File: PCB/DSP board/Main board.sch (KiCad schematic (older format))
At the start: 5 parts, among them X1 Mini_PCI-e

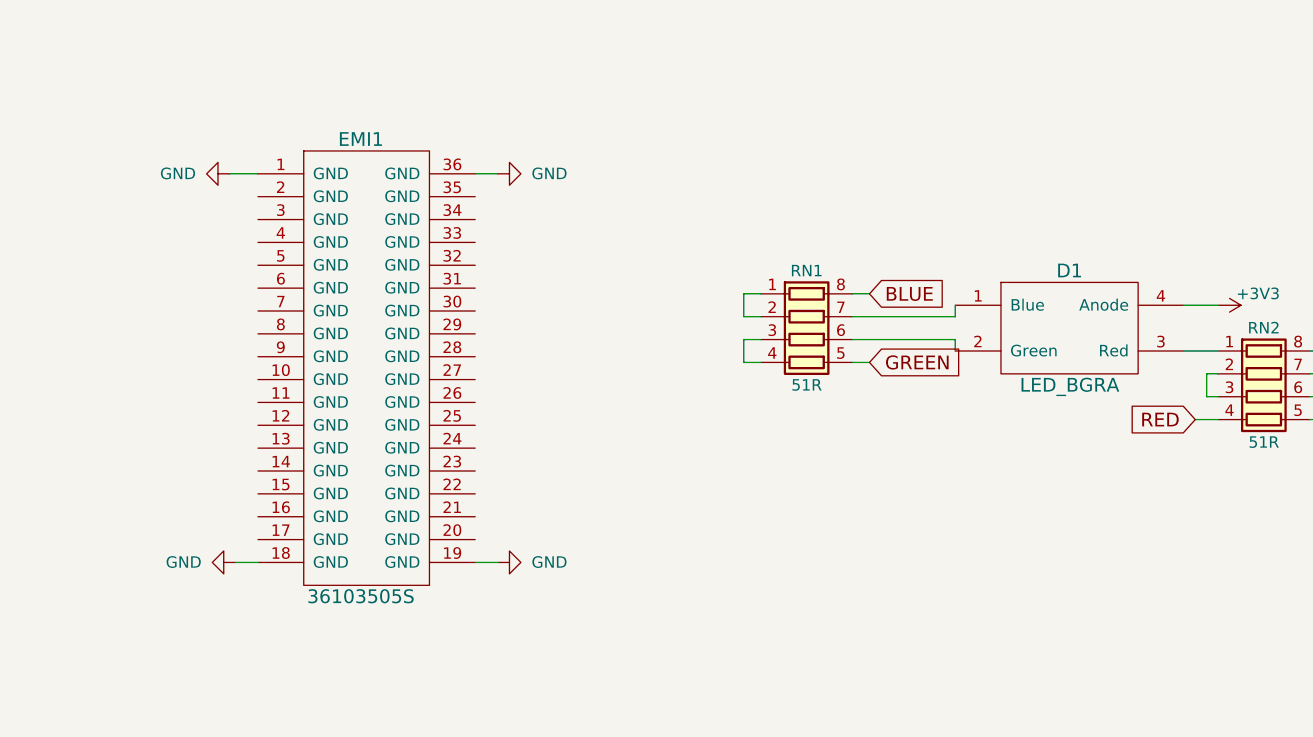
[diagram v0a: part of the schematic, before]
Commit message: Schematics + Footprints Rev.1
Ready to route.
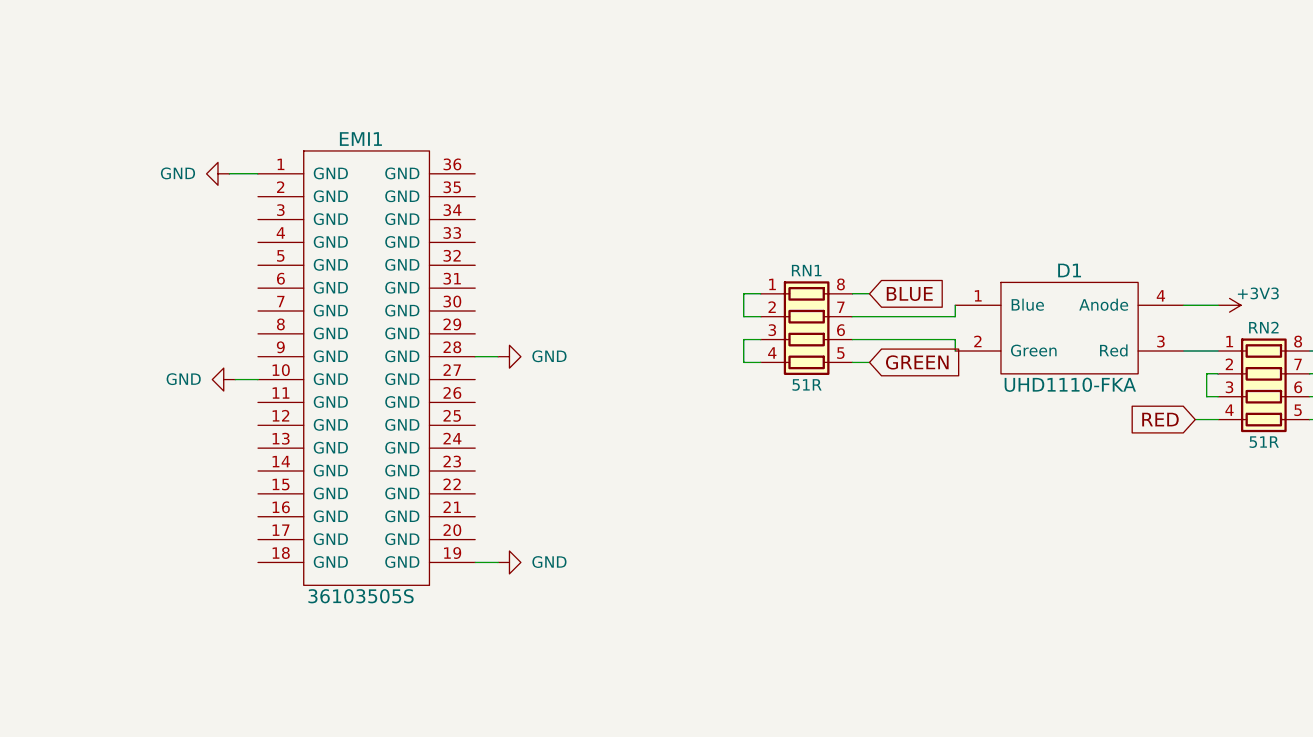
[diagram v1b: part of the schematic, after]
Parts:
- D1: value LED_BGRA -> UHD1110-FKA; footprint (none) -> LED:PLCC-4_1x1mm
- EMI1: footprint (none) -> EMI:36103505S
- RN1, RN2: footprint (none) -> Resistor:0603_RN4
- X1: footprint (none) -> PCI-e:Mini_PCI-e
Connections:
- net GND: now also EMI1.10 (GND), EMI1.28 (GND); no longer EMI1.18 (GND), EMI1.36 (GND)
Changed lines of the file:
@@
 F 0 "X1" H 2800 4400 60  0000 C CNN
 F 1 "Mini_PCI-e" H 2850 2500 60  0000 C CNN
-F 2 "" H 2700 2950 60  0001 C CNN
+F 2 "PCI-e:Mini_PCI-e" H 2700 2950 60  0001 C CNN
 F 3 "" H 2700 2950 60  0001 C CNN
 	1    2800 3450
@@
 F 0 "X1" H 2800 7150 60  0000 C CNN
 F 1 "Mini_PCI-e" H 2850 5250 60  0000 C CNN
-F 2 "" H 2700 5700 60  0001 C CNN
+F 2 "PCI-e:Mini_PCI-e" H 2700 5700 60  0001 C CNN
 F 3 "" H 2700 5700 60  0001 C CNN
 	2    2800 6200
@@
 HRTIM_EEV3
 $Comp
-L GND #PWR1
+L GND #PWR01
 U 1 1 5AB55A4F
 P 3275 2750
-F 0 "#PWR1" H 3275 2500 50  0001 C CNN
+F 0 "#PWR01" H 3275 2500 50  0001 C CNN
 F 1 "GND" V 3275 2525 50  0000 C CNN
 F 2 "" H 3275 2750 50  0001 C CNN
@@
 F 0 "EMI1" H 6075 5150 60  0000 C CNN
 F 1 "36103505S" H 6075 3150 60  0000 C CNN
-F 2 "" H 5575 3950 60  0001 C CNN
+F 2 "EMI:36103505S" H 5575 3950 60  0001 C CNN
 F 3 "" H 5575 3950 60  0001 C CNN
 	1    6075 4150
@@
 $EndComp
 $Comp
-L GND #PWR2
+L GND #PWR02
 U 1 1 5ABA06BB
 P 5500 3300
-F 0 "#PWR2" H 5500 3050 50  0001 C CNN
+F 0 "#PWR02" H 5500 3050 50  0001 C CNN
 F 1 "GND" V 5500 3075 50  0000 C CNN
 F 2 "" H 5500 3300 50  0001 C CNN
@@
 	5500 3300 5625 3300
 $Comp
-L GND #PWR3
+L GND #PWR03
 U 1 1 5ABA072B
-P 5525 5000
-F 0 "#PWR3" H 5525 4750 50  0001 C CNN
-F 1 "GND" V 5525 4775 50  0000 C CNN
-F 2 "" H 5525 5000 50  0001 C CNN
-F 3 "" H 5525 5000 50  0001 C CNN
-	1    5525 5000
+P 5525 4200
+F 0 "#PWR03" H 5525 3950 50  0001 C CNN
+F 1 "GND" V 5525 3975 50  0000 C CNN
+F 2 "" H 5525 4200 50  0001 C CNN
+F 3 "" H 5525 4200 50  0001 C CNN
+	1    5525 4200
 	0    1    1    0
 $EndComp
 $Comp
-L GND #PWR5
+L GND #PWR04
 U 1 1 5ABA0775
 P 6675 5000
-F 0 "#PWR5" H 6675 4750 50  0001 C CNN
+F 0 "#PWR04" H 6675 4750 50  0001 C CNN
 F 1 "GND" V 6675 4775 50  0000 C CNN
 F 2 "" H 6675 5000 50  0001 C CNN
@@
 $EndComp
 $Comp
-L GND #PWR4
+L GND #PWR05
 U 1 1 5ABA07D1
-P 6675 3300
-F 0 "#PWR4" H 6675 3050 50  0001 C CNN
-F 1 "GND" V 6675 3075 50  0000 C CNN
-F 2 "" H 6675 3300 50  0001 C CNN
-F 3 "" H 6675 3300 50  0001 C CNN
-	1    6675 3300
+P 6675 4100
+F 0 "#PWR05" H 6675 3850 50  0001 C CNN
+F 1 "GND" V 6675 3875 50  0000 C CNN
+F 2 "" H 6675 4100 50  0001 C CNN
+F 3 "" H 6675 4100 50  0001 C CNN
+	1    6675 4100
 	0    -1   -1   0
 $EndComp
 Wire Wire Line
-	6575 3300 6675 3300
+	6575 4100 6675 4100
 Wire Wire Line
 	6575 5000 6675 5000
 Wire Wire Line
-	5525 5000 5625 5000
+	5525 4200 5625 4200
 $Comp
 L LED_BGRA D1
@@
 P 9175 3975
 F 0 "D1" H 9175 4225 60  0000 C CNN
-F 1 "LED_BGRA" H 9175 3725 60  0000 C CNN
-F 2 "" H 8875 3975 60  0001 C CNN
+F 1 "UHD1110-FKA" H 9175 3725 60  0000 C CNN
+F 2 "LED:PLCC-4_1x1mm" H 8875 3975 60  0001 C CNN
 F 3 "" H 8875 3975 60  0001 C CNN
 	1    9175 3975
@@
 F 0 "RN1" V 7725 4025 50  0000 C CNN
 F 1 "51R" V 8225 4025 50  0000 C CNN
-F 2 "" V 8300 4025 50  0001 C CNN
+F 2 "Resistor:0603_RN4" V 8300 4025 50  0001 C CNN
 F 3 "" H 8025 4025 50  0001 C CNN
 	1    8025 4025
@@
 F 0 "RN2" V 9725 4275 50  0000 C CNN
 F 1 "51R" V 10225 4275 50  0000 C CNN
-F 2 "" V 10300 4275 50  0001 C CNN
+F 2 "Resistor:0603_RN4" V 10300 4275 50  0001 C CNN
 F 3 "" H 10025 4275 50  0001 C CNN
 	1    10025 4275
@@
 	9725 4375 9825 4375
 $Comp
-L +3V3 #PWR6
+L +3V3 #PWR06
 U 1 1 5AB3F000
 P 9825 3875
-F 0 "#PWR6" H 9825 3725 50  0001 C CNN
+F 0 "#PWR06" H 9825 3725 50  0001 C CNN
 F 1 "+3V3" V 9775 4050 50  0000 C CNN
 F 2 "" H 9825 3875 50  0001 C CNN

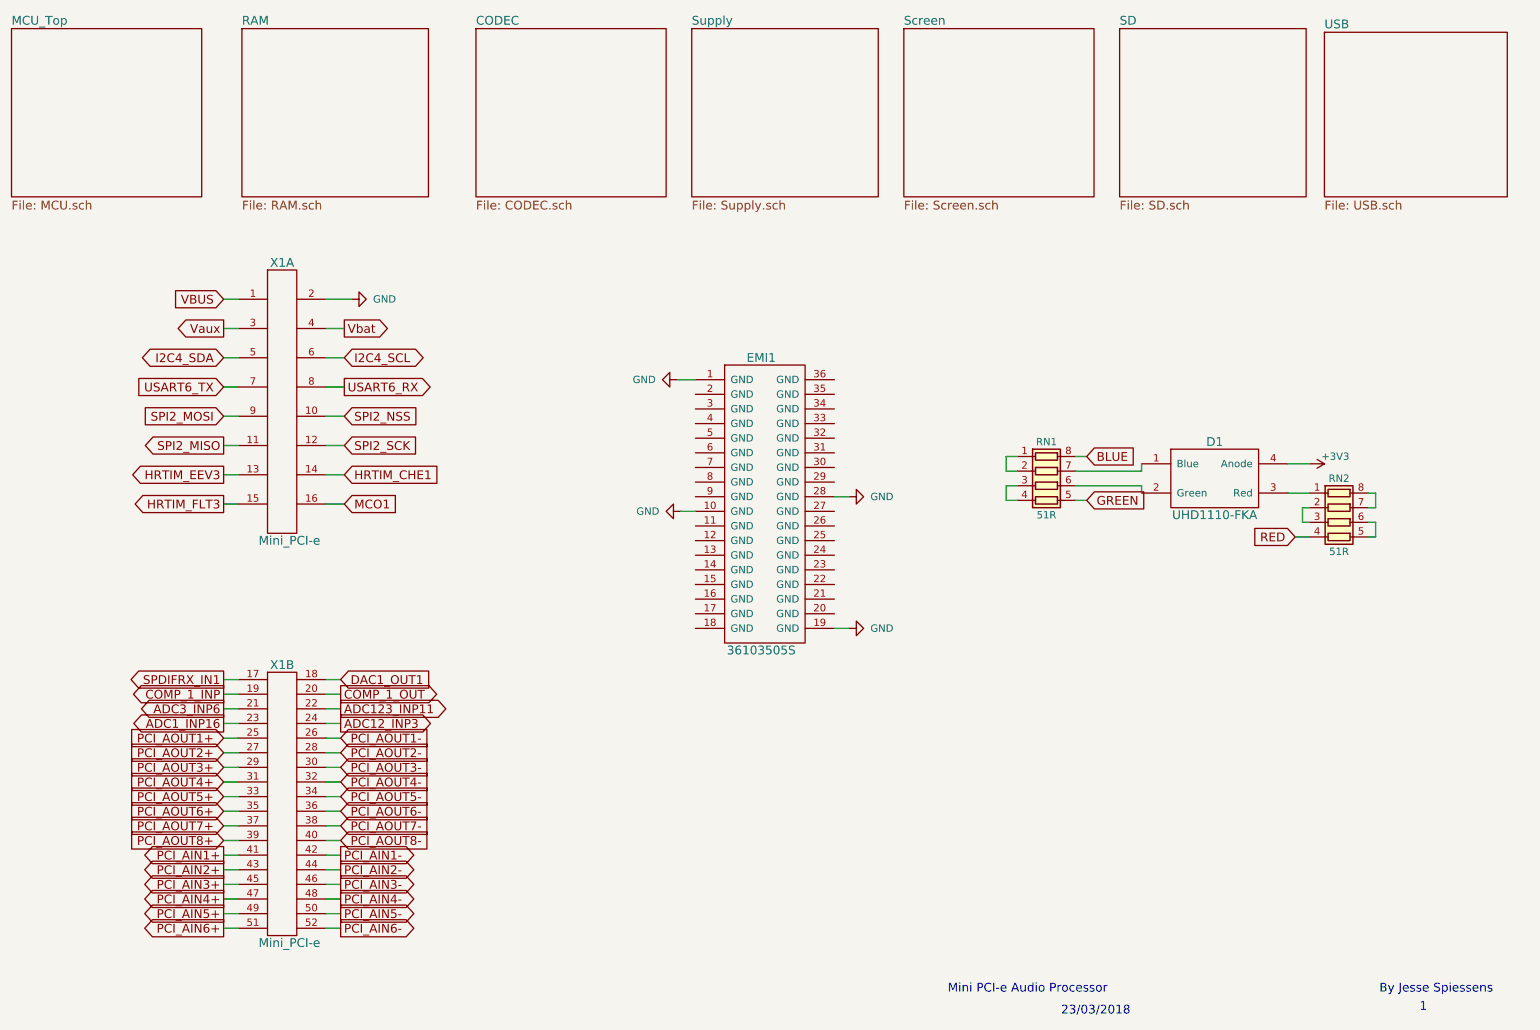
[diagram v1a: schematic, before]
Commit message: Schematics & PCB
Schematics update - ERC error fixing
PCB - setup & PCB outline
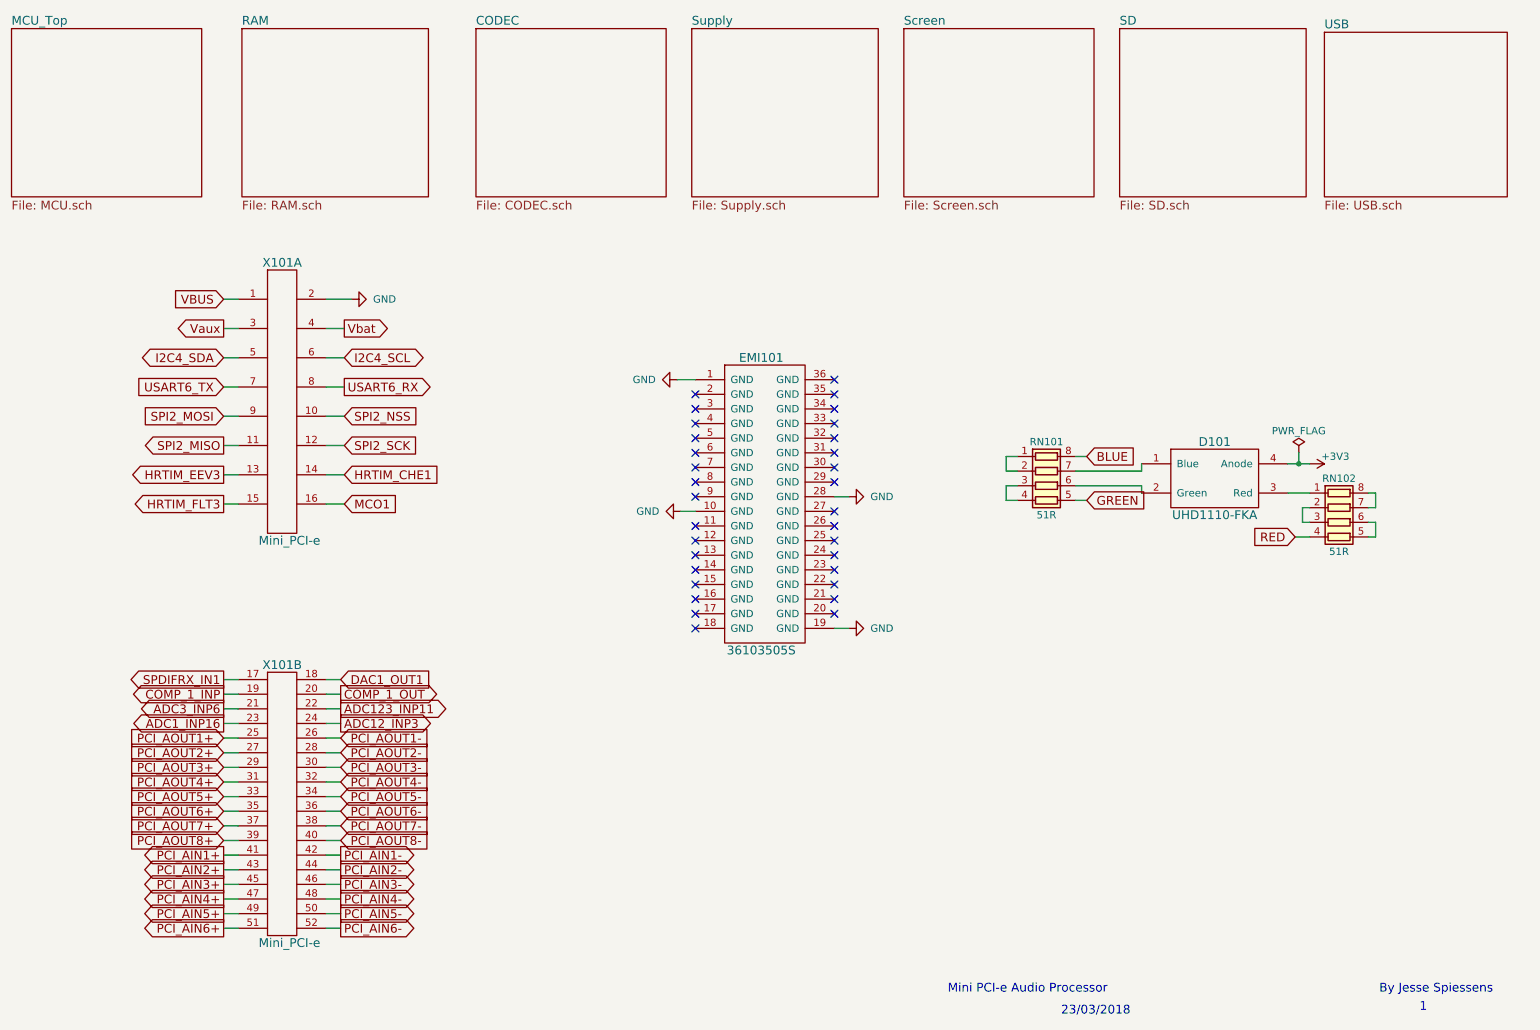
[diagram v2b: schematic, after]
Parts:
- renumbered D1 to D101, EMI1 to EMI101, RN1 to RN101, RN2 to RN102, X1 to X101
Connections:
- no-connect marks 0 -> 32
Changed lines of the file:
@@
 $EndSheet
 $Comp
-L Mini_PCI-e X1
+L Mini_PCI-e X101
 U 1 1 5AB547B6
 P 2800 3450
-F 0 "X1" H 2800 4400 60  0000 C CNN
+F 0 "X101" H 2800 4400 60  0000 C CNN
 F 1 "Mini_PCI-e" H 2850 2500 60  0000 C CNN
 F 2 "PCI-e:Mini_PCI-e" H 2700 2950 60  0001 C CNN
@@
 $EndComp
 $Comp
-L Mini_PCI-e X1
+L Mini_PCI-e X101
 U 2 1 5AB54885
 P 2800 6200
-F 0 "X1" H 2800 7150 60  0000 C CNN
+F 0 "X101" H 2800 7150 60  0000 C CNN
 F 1 "Mini_PCI-e" H 2850 5250 60  0000 C CNN
 F 2 "PCI-e:Mini_PCI-e" H 2700 5700 60  0001 C CNN
@@
 	3100 5350 3200 5350
 $Comp
-L 36103505S EMI1
+L 36103505S EMI101
 U 1 1 5ABA05A0
 P 6075 4150
-F 0 "EMI1" H 6075 5150 60  0000 C CNN
+F 0 "EMI101" H 6075 5150 60  0000 C CNN
 F 1 "36103505S" H 6075 3150 60  0000 C CNN
 F 2 "EMI:36103505S" H 5575 3950 60  0001 C CNN
@@
 	5525 4200 5625 4200
 $Comp
-L LED_BGRA D1
+L LED_BGRA D101
 U 1 1 5AB3DEEC
 P 9175 3975
-F 0 "D1" H 9175 4225 60  0000 C CNN
+F 0 "D101" H 9175 4225 60  0000 C CNN
 F 1 "UHD1110-FKA" H 9175 3725 60  0000 C CNN
 F 2 "LED:PLCC-4_1x1mm" H 8875 3975 60  0001 C CNN
@@
 $EndComp
 $Comp
-L R_Pack04 RN1
+L R_Pack04 RN101
 U 1 1 5AB3E0B3
 P 8025 4025
-F 0 "RN1" V 7725 4025 50  0000 C CNN
+F 0 "RN101" V 7725 4025 50  0000 C CNN
 F 1 "51R" V 8225 4025 50  0000 C CNN
 F 2 "Resistor:0603_RN4" V 8300 4025 50  0001 C CNN
@@
 	8225 3825 8300 3825
 $Comp
-L R_Pack04 RN2
+L R_Pack04 RN102
 U 1 1 5AB3E8CF
 P 10025 4275
-F 0 "RN2" V 9725 4275 50  0000 C CNN
+F 0 "RN102" V 9725 4275 50  0000 C CNN
 F 1 "51R" V 10225 4275 50  0000 C CNN
 F 2 "Resistor:0603_RN4" V 10300 4275 50  0001 C CNN
@@
 Text Notes 10300 7500 0    60   ~ 0
 By Jesse Spiessens
+NoConn ~ 5625 3400
+NoConn ~ 5625 3500
+NoConn ~ 5625 3600
+NoConn ~ 5625 3700
+NoConn ~ 5625 3800
+NoConn ~ 5625 3900
+NoConn ~ 5625 4000
+NoConn ~ 5625 4100
+NoConn ~ 5625 4300
+NoConn ~ 5625 4400
+NoConn ~ 5625 4500
+NoConn ~ 5625 4600
+NoConn ~ 5625 4700
+NoConn ~ 5625 4800
+NoConn ~ 5625 4900
+NoConn ~ 5625 5000
+NoConn ~ 6575 3300
+NoConn ~ 6575 3400
+NoConn ~ 6575 3500
+NoConn ~ 6575 3600
+NoConn ~ 6575 3700
+NoConn ~ 6575 3800
+NoConn ~ 6575 3900
+NoConn ~ 6575 4000
+NoConn ~ 6575 4200
+NoConn ~ 6575 4300
+NoConn ~ 6575 4400
+NoConn ~ 6575 4500
+NoConn ~ 6575 4600
+NoConn ~ 6575 4700
+NoConn ~ 6575 4800
+NoConn ~ 6575 4900
+$Comp
+L PWR_FLAG #FLG07
+U 1 1 5ABDE685
+P 9750 3800
+F 0 "#FLG07" H 9750 3875 50  0001 C CNN
+F 1 "PWR_FLAG" H 9750 3950 50  0000 C CNN
+F 2 "" H 9750 3800 50  0001 C CNN
+F 3 "" H 9750 3800 50  0001 C CNN
+	1    9750 3800
+	1    0    0    -1
+$EndComp
+Wire Wire Line
+	9750 3800 9750 3875
+Connection ~ 9750 3875
 $EndSCHEMATC

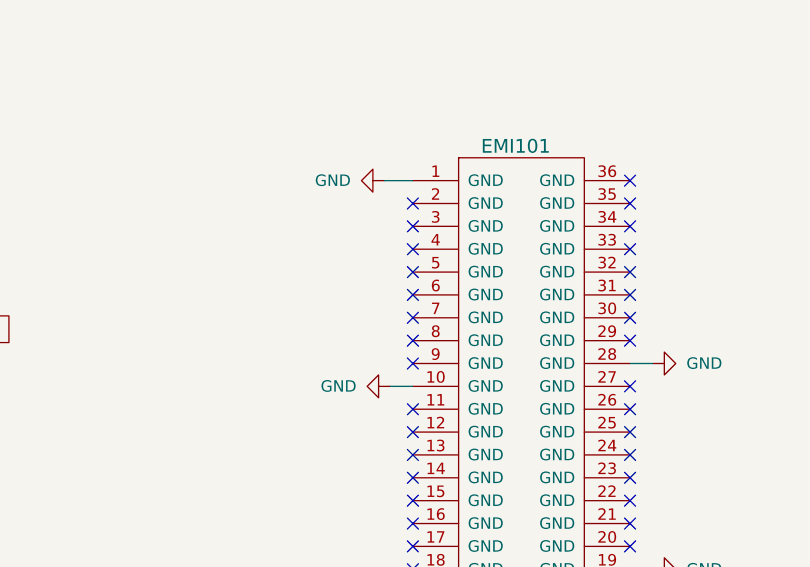
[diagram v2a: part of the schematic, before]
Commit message: RAM Routing - Data
All RAM routing & matching done, supply still needs to be done
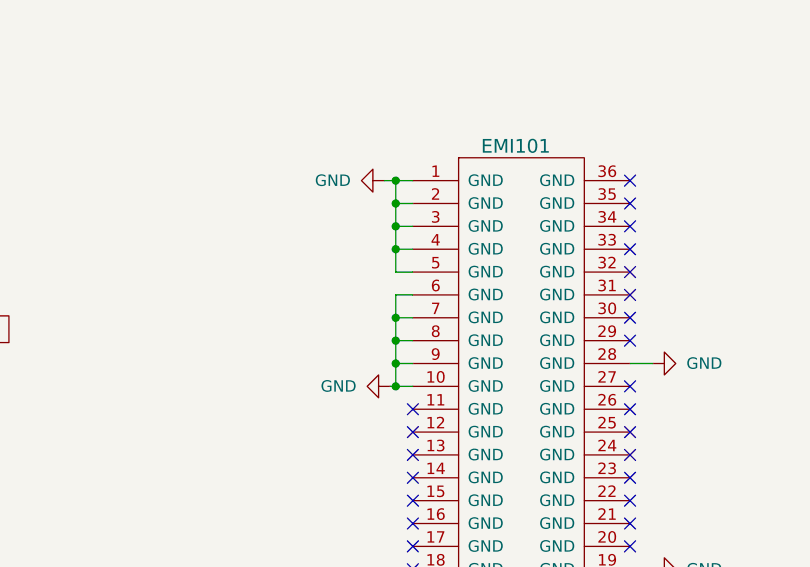
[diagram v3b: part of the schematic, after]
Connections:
- net GND: now also EMI101.2 (GND), EMI101.3 (GND), EMI101.4 (GND), EMI101.5 (GND), EMI101.6 (GND), EMI101.7 (GND), EMI101.8 (GND), EMI101.9 (GND)
- no-connect marks 32 -> 24
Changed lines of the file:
@@
 Text Notes 10300 7500 0    60   ~ 0
 By Jesse Spiessens
-NoConn ~ 5625 3400
-NoConn ~ 5625 3500
-NoConn ~ 5625 3600
-NoConn ~ 5625 3700
-NoConn ~ 5625 3800
-NoConn ~ 5625 3900
-NoConn ~ 5625 4000
-NoConn ~ 5625 4100
 NoConn ~ 5625 4300
 NoConn ~ 5625 4400
@@
 	9750 3800 9750 3875
 Connection ~ 9750 3875
+Wire Wire Line
+	5550 3300 5550 3700
+Wire Wire Line
+	5550 3400 5625 3400
+Connection ~ 5550 3300
+Wire Wire Line
+	5550 3500 5625 3500
+Connection ~ 5550 3400
+Wire Wire Line
+	5550 3600 5625 3600
+Connection ~ 5550 3500
+Wire Wire Line
+	5550 3700 5625 3700
+Connection ~ 5550 3600
+Wire Wire Line
+	5625 4100 5550 4100
+Wire Wire Line
+	5550 3800 5550 4200
+Connection ~ 5550 4200
+Wire Wire Line
+	5625 4000 5550 4000
+Connection ~ 5550 4100
+Wire Wire Line
+	5625 3900 5550 3900
+Connection ~ 5550 4000
+Wire Wire Line
+	5625 3800 5550 3800
+Connection ~ 5550 3900
 $EndSCHEMATC

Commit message: Routing done Rev 1
Still need to add some testpoints and art
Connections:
- net +3V3 renamed +3V3_MCU
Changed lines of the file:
@@
 Text GLabel 9725 4375 0    60   Input ~ 0
 RED
-$Comp
-L +3V3 #PWR06
-U 1 1 5AB3F000
-P 9825 3875
-F 0 "#PWR06" H 9825 3725 50  0001 C CNN
-F 1 "+3V3" V 9775 4050 50  0000 C CNN
-F 2 "" H 9825 3875 50  0001 C CNN
-F 3 "" H 9825 3875 50  0001 C CNN
-	1    9825 3875
-	0    1    1    0
-$EndComp
 Text GLabel 2400 4150 0    60   Output ~ 0
 HRTIM_FLT3
@@
 	5625 3800 5550 3800
 Connection ~ 5550 3900
+Text GLabel 9825 3875 2    60   Input ~ 0
++3V3_MCU
 $EndSCHEMATC
